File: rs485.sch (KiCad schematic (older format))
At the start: 17 parts, among them J1 Screw_Terminal_1x02, J2 Screw_Terminal_1x02, J3 CONN_01X03, J4 CONN_01X06, U1 MAX485E

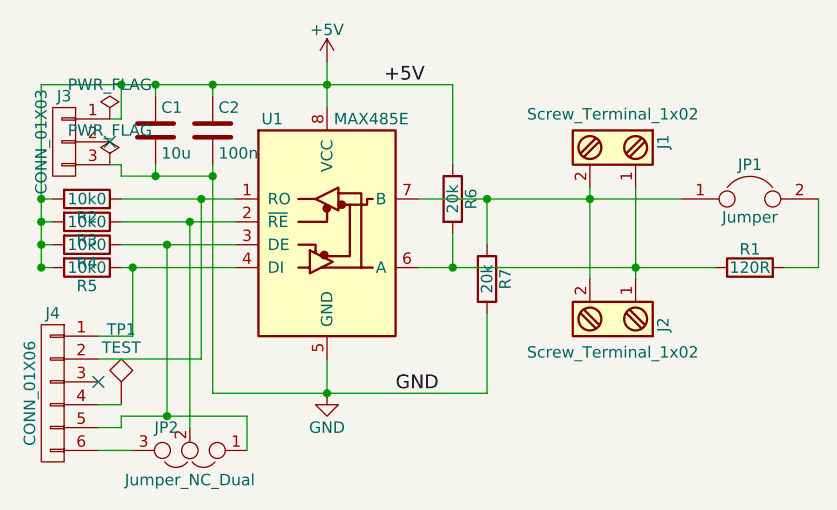
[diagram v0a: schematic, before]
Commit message: Changed BOM
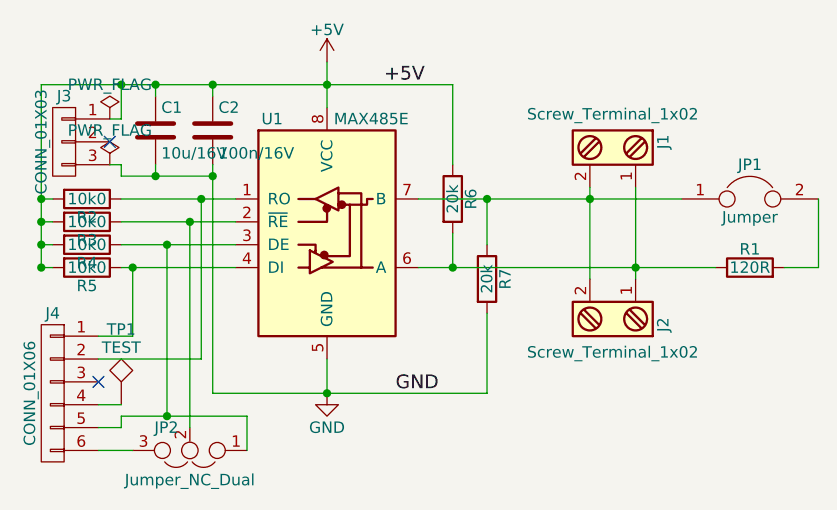
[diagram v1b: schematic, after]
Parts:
- C1: value 10u -> 10u/16V; Aliexpress link (none) -> https://www.aliexpress.com/item/Free-shipping-1206-SMD-capa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; Unit price $ (none) -> 0.02
- C2: value 100n -> 100n/16V; Aliexpress link (none) -> https://www.aliexpress.com/item/0603-SMD-Capacitor-assorted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; Unit price $ (none) -> 0.01
- J1: Aliexpress link (none) -> https://www.aliexpress.com/item/50-pcs-Universal-2-54-mm-Pi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; Unit price $ (none) -> 0.20
- J3: Aliexpress link (none) -> https://www.aliexpress.com/item/Hot-Sale10pcs-40-Pin-1x40-S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; Unit price $ (none) -> 0.004
- J4: Unit price $ (none) -> 0.008
- JP1, R1, R6: Unit price $ (none) -> 0.003
- JP2, TP1: Unit price $ (none) -> 0.00
- R2: Aliexpress link (none) -> https://www.aliexpress.com/item/Free-shipping-Hot-sale-0603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; Unit price $ (none) -> 0.003
- U1: Aliexpress link (none) -> https://www.aliexpress.com/item/XIN-YANG-Electronic-NEW-ORI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; Unit price $ (none) -> 0.60
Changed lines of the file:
@@
 F 1 "MAX485E" H 3330 2550 50  0000 L CNN
 F 2 "Housings_SOIC:SOIC-8_3.9x4.9mm_Pitch1.27mm" H 3300 1400 50  0001 C CNN
-F 3 "" H 3300 2150 50  0001 C CNN
+F 3 "https://datasheets.maximintegrated.com/en/ds/MAX1487-MAX491.pdf" H 3300 2150 50  0001 C CNN
+F 4 "https://www.aliexpress.com/item/XIN-YANG-Electronic-NEW-ORIGINAL-MAX485CSA-T-MAX485CSA-MAX485-SOP-MAXIM-Free-shipping/32355724259.html" H 3300 2100 60  0001 C CNN "Aliexpress link"
+F 5 "0.60" H 3300 2100 60  0001 C CNN "Unit price $"
 	1    3300 2100
 	1    0    0    -1
@@
 F 2 "Connectors_Terminal_Blocks:TerminalBlock_Pheonix_MPT-2.54mm_2pol" H 4550 1525 50  0001 C CNN
 F 3 "" H 4525 1750 50  0001 C CNN
+F 4 "https://www.aliexpress.com/item/50-pcs-Universal-2-54-mm-Pitch-2-Pin-3-4-5-6-7-8-9/32809307718.html" H 4550 1750 60  0001 C CNN "Aliexpress link"
+F 5 "0.20" H 4550 1750 60  0001 C CNN "Unit price $"
 	1    4550 1750
 	0    1    1    0
@@
 F 2 "Pin_Headers:Pin_Header_Straight_1x02_Pitch2.54mm" H 5150 2000 50  0001 C CNN
 F 3 "" H 5150 2000 50  0001 C CNN
+F 4 "0.003" H 5150 2000 60  0001 C CNN "Unit price $"
 	1    5150 2000
 	1    0    0    -1
@@
 F 2 "Resistors_SMD:R_0603" V 5080 2300 50  0001 C CNN
 F 3 "" H 5150 2300 50  0001 C CNN
+F 4 "0.003" V 5150 2300 60  0001 C CNN "Unit price $"
 	1    5150 2300
 	0    -1   -1   0
@@
 F 2 "Resistors_SMD:R_0603" V 2180 2000 50  0001 C CNN
 F 3 "" H 2250 2000 50  0001 C CNN
+F 4 "https://www.aliexpress.com/item/Free-shipping-Hot-sale-0603-SMD-Resistor-Kit-Assorted-Kit-1ohm-10M-ohm-1-36valuesX20pcs-720pcs/32359683117.html" V 2250 2000 60  0001 C CNN "Aliexpress link"
+F 5 "0.003" V 2250 2000 60  0001 C CNN "Unit price $"
 	1    2250 2000
 	0    1    1    0
@@
 F 2 "Resistors_SMD:R_0603" V 3780 2000 50  0001 C CNN
 F 3 "" H 3850 2000 50  0001 C CNN
+F 4 "0.003" V 3850 2000 60  0001 C CNN "Unit price $"
 	1    3850 2000
 	1    0    0    -1
@@
 P 2550 1700
 F 0 "C1" H 2575 1800 50  0000 L CNN
-F 1 "10u" H 2575 1600 50  0000 L CNN
+F 1 "10u/16V" H 2575 1600 50  0000 L CNN
 F 2 "Capacitors_SMD:C_1206" H 2588 1550 50  0001 C CNN
 F 3 "" H 2550 1700 50  0001 C CNN
+F 4 "https://www.aliexpress.com/item/Free-shipping-1206-SMD-capacitor-10UF-25V-106M-100PCS/32371669400.html" H 2550 1700 60  0001 C CNN "Aliexpress link"
+F 5 "0.02" H 2550 1700 60  0001 C CNN "Unit price $"
 	1    2550 1700
 	1    0    0    -1
@@
 P 2800 1700
 F 0 "C2" H 2825 1800 50  0000 L CNN
-F 1 "100n" H 2825 1600 50  0000 L CNN
+F 1 "100n/16V" H 2825 1600 50  0000 L CNN
 F 2 "Capacitors_SMD:C_0603" H 2838 1550 50  0001 C CNN
 F 3 "" H 2800 1700 50  0001 C CNN
+F 4 "https://www.aliexpress.com/item/0603-SMD-Capacitor-assorted-kit-52values-25pcs-1300pcs-1pF-1uF-Samples-kit/1727377024.html" H 2800 1700 60  0001 C CNN "Aliexpress link"
+F 5 "0.01" H 2800 1700 60  0001 C CNN "Unit price $"
 	1    2800 1700
 	1    0    0    -1
@@
 F 2 "Pin_Headers:Pin_Header_Straight_1x03_Pitch2.54mm" H 2150 1750 50  0001 C CNN
 F 3 "" H 2150 1750 50  0001 C CNN
+F 4 "https://www.aliexpress.com/item/Hot-Sale10pcs-40-Pin-1x40-Single-Row-Male-2-54-Breakable-Pin-Header-Connector-Strip-for/32374809500.html" H 2150 1750 60  0001 C CNN "Aliexpress link"
+F 5 "0.004" H 2150 1750 60  0001 C CNN "Unit price $"
 	1    2150 1750
 	-1   0    0    -1
@@
 F 2 "Connectors:GS3" H 2700 3100 50  0001 C CNN
 F 3 "" H 2700 3100 50  0001 C CNN
+F 4 "0.00" H 2700 3100 60  0001 C CNN "Unit price $"
 	1    2700 3100
 	-1   0    0    1
@@
 F 2 "Pin_Headers:Pin_Header_Straight_1x06_Pitch2.54mm" H 2100 2850 50  0001 C CNN
 F 3 "" H 2100 2850 50  0001 C CNN
+F 4 "0.008" H 2100 2850 60  0001 C CNN "Unit price $"
 	1    2100 2850
 	-1   0    0    -1
@@
 F 2 "Measurement_Points:Measurement_Point_Round-SMD-Pad_Small" H 2400 2900 50  0001 C CNN
 F 3 "" H 2400 2900 50  0001 C CNN
+F 4 "0.00" H 2400 2900 60  0001 C CNN "Unit price $"
 	1    2400 2900
 	1    0    0    -1
